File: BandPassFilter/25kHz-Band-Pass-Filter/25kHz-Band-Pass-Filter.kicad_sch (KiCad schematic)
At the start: 68 parts, among them J1 Conn_01x02, J2 Conn_01x02, J3 Conn_01x02, J4 Conn_01x02, U1 ${SIM.PARAMS}, U10 ${SIM.PARAMS}, U11 ${SIM.PARAMS}, U12 ${SIM.PARAMS}, U13 ${SIM.PARAMS}, U14 LTC2171CUKG-14_PBF, U2 ${SIM.PARAMS}, U3 ${SIM.PARAMS}, U4 MCP6S21-I_SN, U5 ${SIM.PARAMS}, U6 ${SIM.PARAMS}, U7 ${SIM.PARAMS}, U8 ${SIM.PARAMS}, U9 ${SIM.PARAMS}

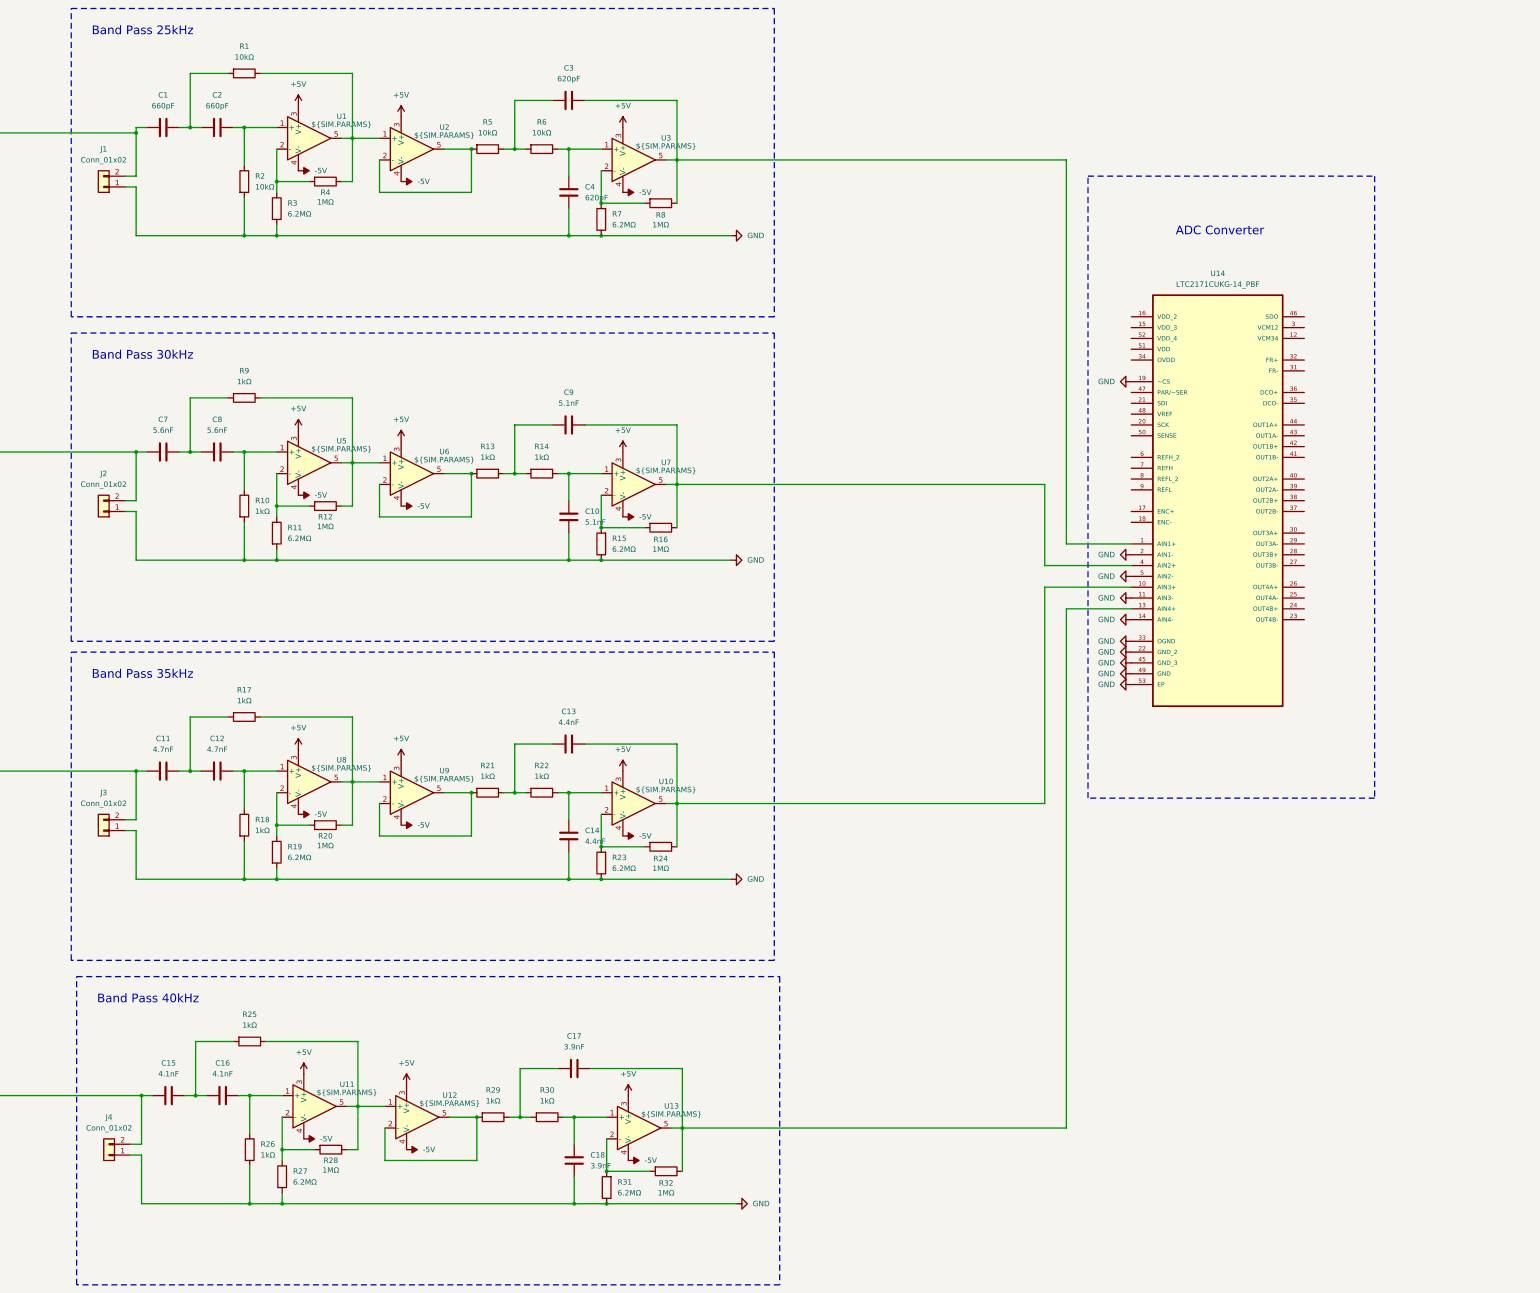
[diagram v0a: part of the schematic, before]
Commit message: Added Schematics for Input Filter
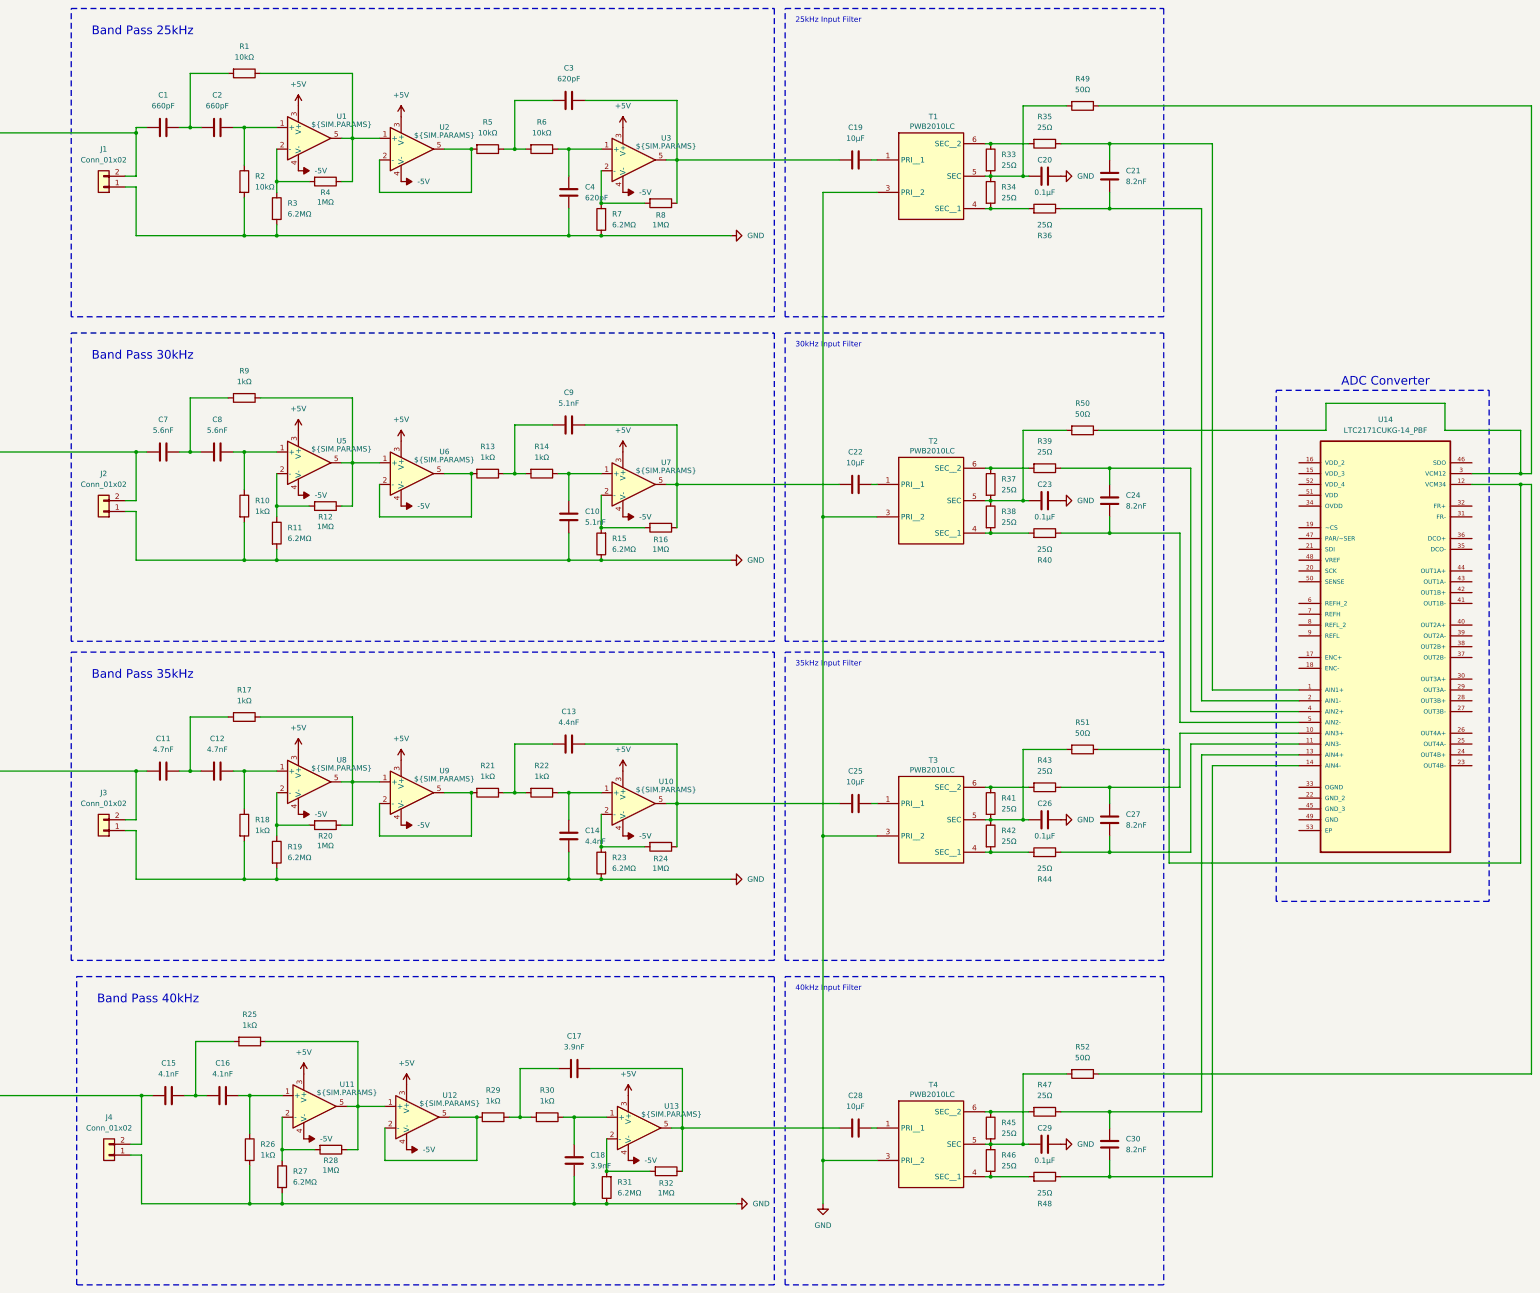
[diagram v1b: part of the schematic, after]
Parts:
- added C19, C22, C25, C28: 10µF, symbol Device:C
- added C20, C23, C26, C29: 0.1µF, symbol Device:C
- added C21, C24, C27, C30: 8.2nF, symbol Device:C
- added R33, R34, R35, R36, R37, R38, R39, R40, R41, R42, R43, R44, R45, R46, R47, R48: 25Ω, symbol Device:R
- added R49, R50, R51, R52: 50Ω, symbol Device:R
- added T1, T2, T3, T4: PWB2010LC, PWB2010LC, symbol PWB2010LC:PWB2010LC
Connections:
- net GND: now also C20.1, C23.1, C26.1, C29.1, T1.3 (PRI__2), T2.3 (PRI__2), T3.3 (PRI__2), T4.3 (PRI__2); no longer U14.11 (AIN3-), U14.14 (AIN4-), U14.19 (~CS), U14.2 (AIN1-), U14.22 (GND_2), U14.33 (OGND), U14.45 (GND_3), U14.49 (GND), U14.5 (AIN2-), U14.53 (EP)
- net at C9.1, R16.1, U7.5: now also C22.2; no longer U14.4 (AIN2+)
- net at C3.1, R8.1, U3.5: now also C19.2; no longer U14.1 (AIN1+)
- net at C13.1, R24.1, U10.5: now also C25.2; no longer U14.10 (AIN3+)
- net at U14.12 (VCM34): now also R51.1, R52.1
- net at C17.1, R32.1, U13.5: now also C28.2; no longer U14.13 (AIN4+)
- net at U14.3 (VCM12): now also R49.1, R50.1
- new net: C22.1, T2.1 (PRI__1)
- new net: R38.2, R40.2, T2.4 (SEC__1)
- new net: C23.2, R37.2, R38.1, R50.2, T2.5 (SEC)
- new net: R37.1, R39.2, T2.6 (SEC__2)
- new net: C29.2, R45.2, R46.1, R52.2, T4.5 (SEC)
- new net: R46.2, R48.2, T4.4 (SEC__1)
- new net: C20.2, R33.2, R34.1, R49.2, T1.5 (SEC)
- new net: R34.2, R36.2, T1.4 (SEC__1)
- new net: C21.1, R35.1, U14.1 (AIN1+)
- new net: C27.1, R43.1, U14.10 (AIN3+)
- new net: C27.2, R44.1, U14.11 (AIN3-)
- new net: C30.1, R47.1, U14.13 (AIN4+)
- new net: C30.2, R48.1, U14.14 (AIN4-)
- new net: C21.2, R36.1, U14.2 (AIN1-)
- new net: C24.1, R39.1, U14.4 (AIN2+)
- new net: C24.2, R40.1, U14.5 (AIN2-)
- new net: C19.1, T1.1 (PRI__1)
- new net: R42.2, R44.2, T3.4 (SEC__1)
- new net: C26.2, R41.2, R42.1, R51.2, T3.5 (SEC)
- new net: R45.1, R47.2, T4.6 (SEC__2)
- new net: R33.1, R35.2, T1.6 (SEC__2)
- new net: C28.1, T4.1 (PRI__1)
- new net: C25.1, T3.1 (PRI__1)
- new net: R41.1, R43.2, T3.6 (SEC__2)
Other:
- note added: "25kHz Input Filter"
- note added: "30kHz Input Filter"
- note added: "35kHz Input Filter"
- note added: "40kHz Input Filter"
- moved on the sheet: U14
